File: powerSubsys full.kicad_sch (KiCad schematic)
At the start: 67 parts, among them J1 Conn_02x16_Odd_Even, J2 JST_PH_2mm, Q1 PN2222A, Q3 IRLML6402, U1 INA219AxD, U10 TPS63020DSJR, U2 DRV8833PWR, U3 BQ24074RGT, U4 TPS22810DRV, U5 TPS22810DRV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

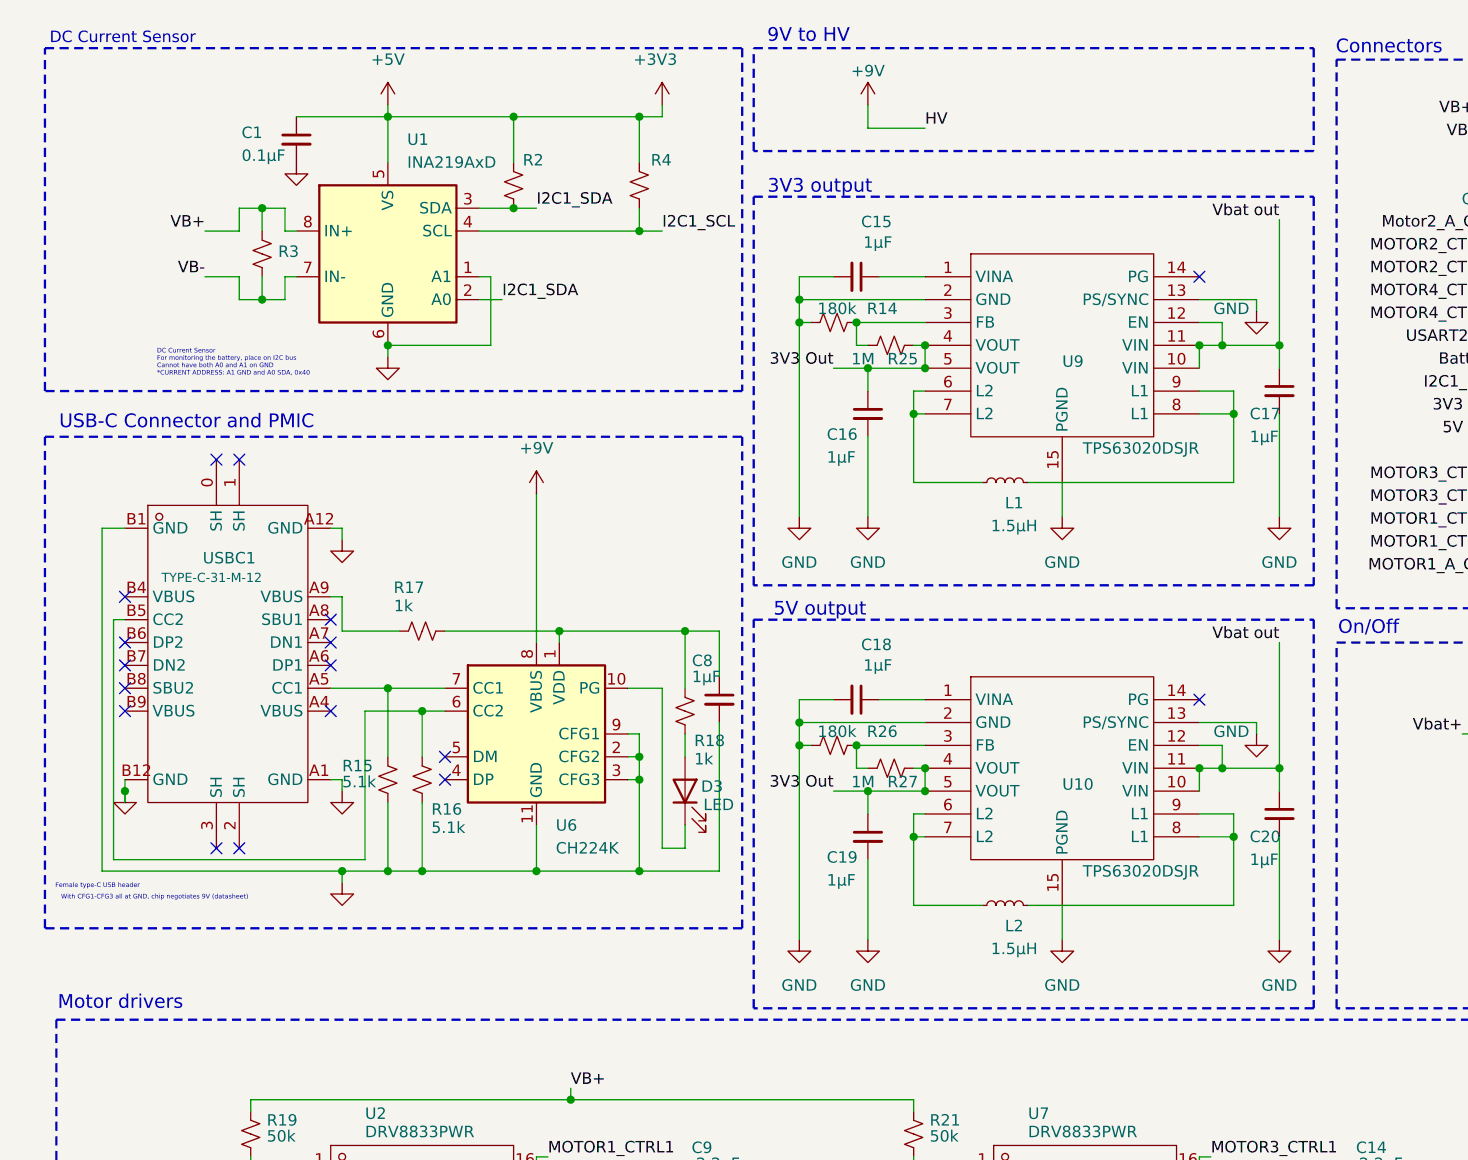
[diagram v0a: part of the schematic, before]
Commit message: Added 3V3 and 5V Output
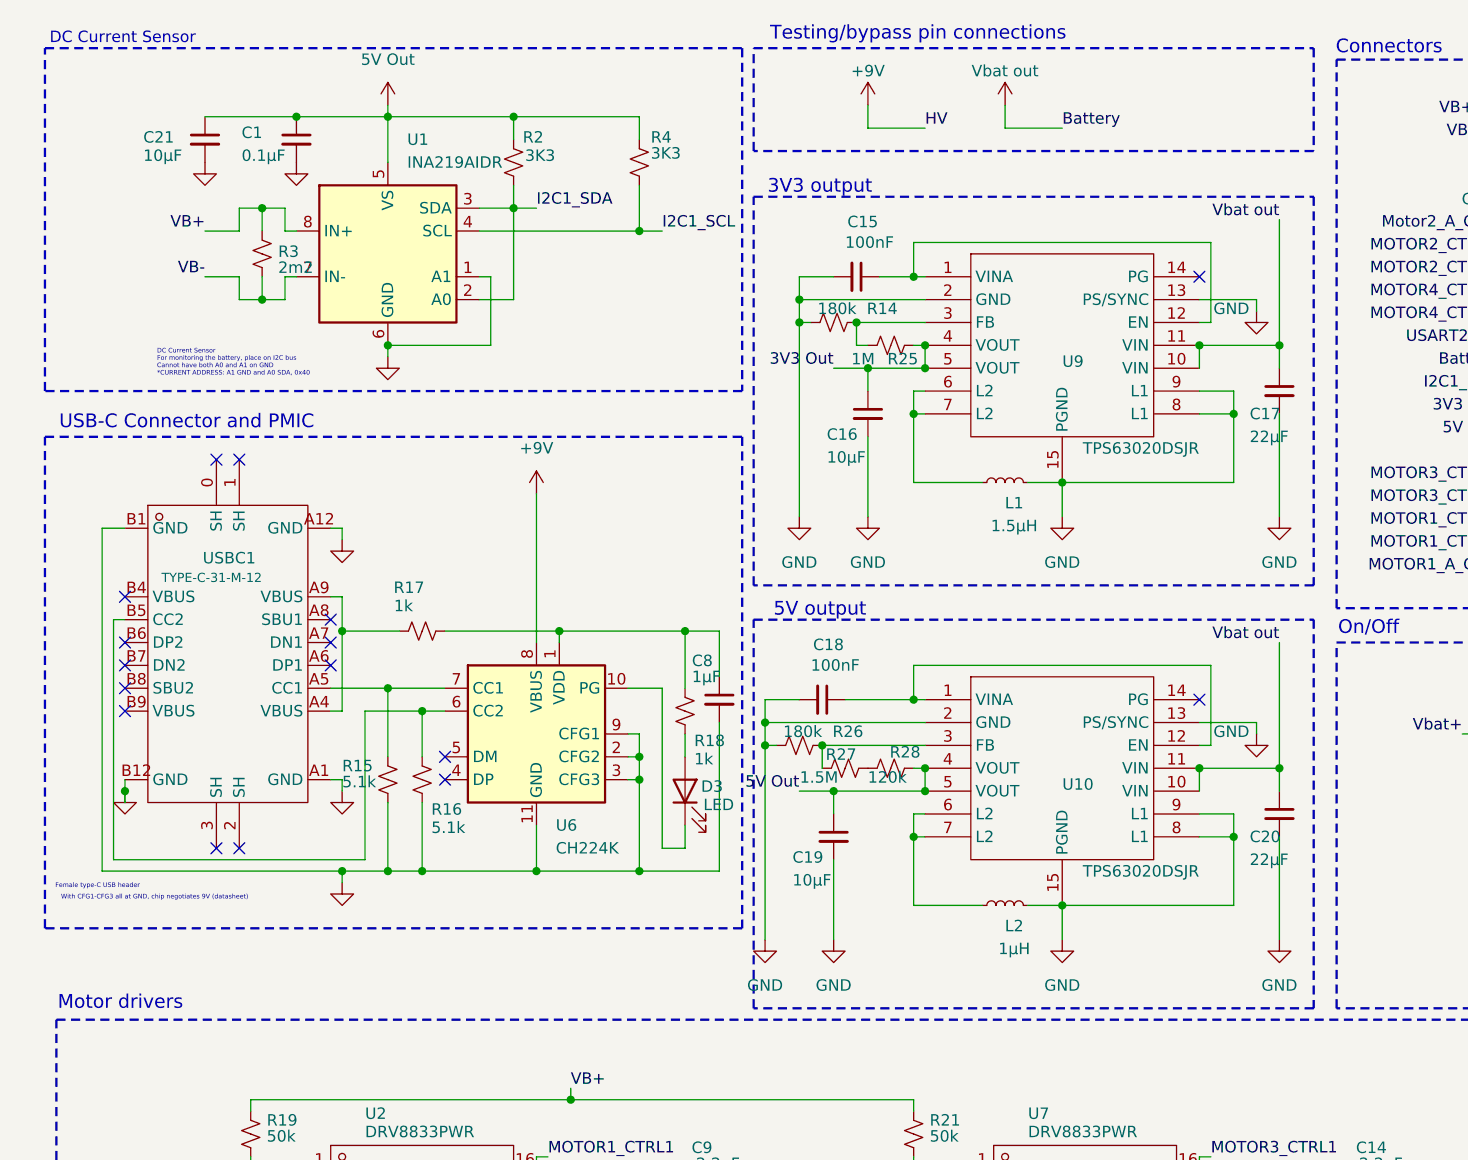
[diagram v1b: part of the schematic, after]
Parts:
- added C21: 10μF, symbol Device:C_Small
- added R28: 120k, symbol Device:R_Small_US
- C15, C18: value 1μF -> 100nF
- C16, C19: value 1μF -> 10μF
- C17, C20: value 1μF -> 22μF
- L2: value 1.5μH -> 1μH
- R2, R4: value R_Small_US -> 3K3
- R27: value 1M -> 1.5M
- R3: value R_Small_US -> 2m2
- U1: value INA219AxD -> INA219AIDR
- U10, U9: footprint VSON-14_L4.0-W3.0-P0.50-BL-EP_TI_DSJ -> Library:VSON-14_L4.0-W3.0-P0.50-BL-EP_TI_DSJ
- U2, U7: footprint TSSOP-16_L5.0-W4.4-P0.65-LS6.4-BL -> Library:TSSOP-16_L5.0-W4.4-P0.65-LS6.4-BL
- USBC1: footprint USB-C_SMD-TYPE-C-31-M-12 -> Library:USB-C_SMD-TYPE-C-31-M-12
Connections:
- net +3V3 is gone; now on net 5V Out: C1.1, R2.1, R4.1, U1.5 (VS)
- net Battery is gone; now on net Vbat out: J1.14 (Pin_14)
- net 3V3 Out: no longer C19.1, R27.2, U10.4 (VOUT), U10.5 (VOUT)
- net 5V Out: now also C19.1, U10.4 (VOUT), U10.5 (VOUT), C21.1, R28.2
- net GND: now also L1.2, L2.2, U10.8 (L1), U10.9 (L1), U9.8 (L1), U9.9 (L1), C21.2
- net Vbat out: no longer U10.12 (EN), U9.12 (EN)
- net at C18.1, U10.1 (VINA): now also U10.12 (EN)
- net at R17.1, USBC1.A9 (VBUS): now also USBC1.A4 (VBUS)
- net at C15.1, U9.1 (VINA): now also U9.12 (EN)
- new net: R27.2, R28.1
- no-connect marks 21 -> 20
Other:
- note added: "Testing/bypass pin connections"
- note removed: "9V to HV"
- moved on the sheet: R2, R4

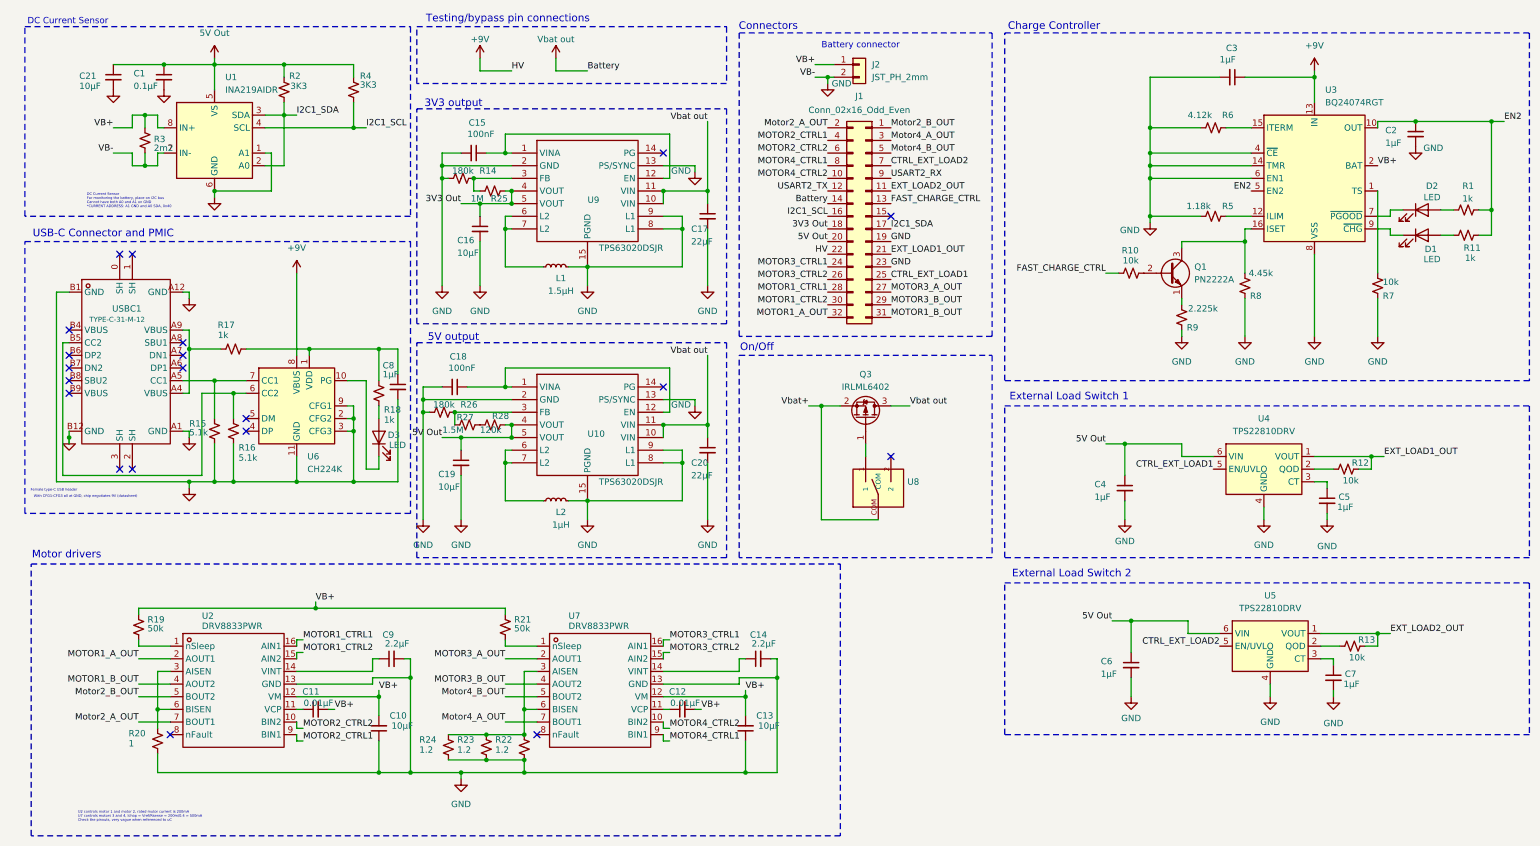
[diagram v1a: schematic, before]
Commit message: Updated the switch design
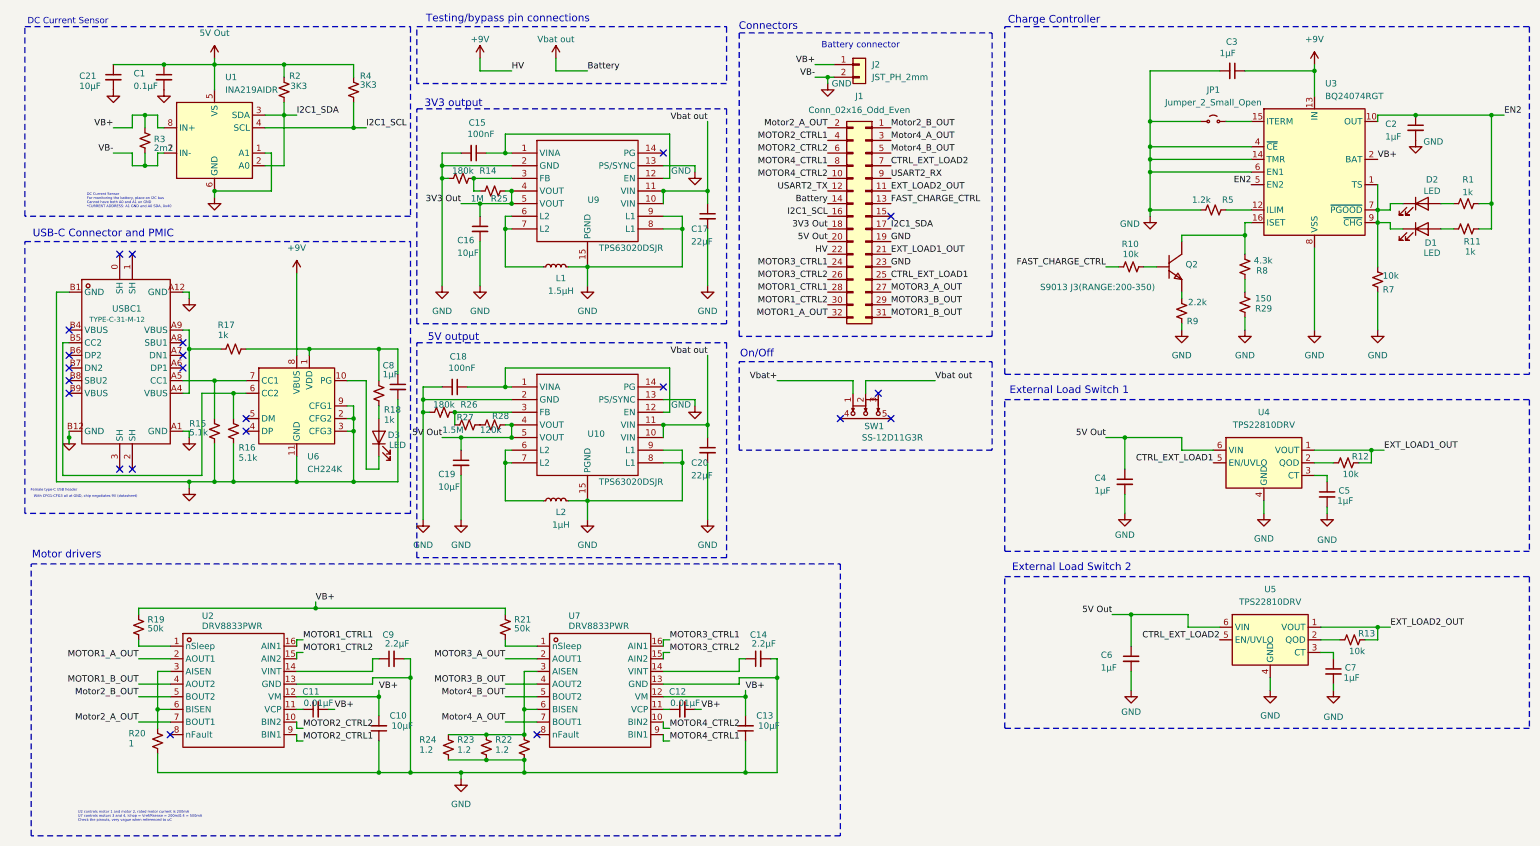
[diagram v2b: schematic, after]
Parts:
- removed Q1: PN2222A, Package_TO_SOT_THT:TO-92_Inline, symbol Transistor_BJT:PN2222A
- removed Q3: IRLML6402, Package_TO_SOT_SMD:SOT-23, symbol Transistor_FET:IRLML6402
- removed R6: 4.12k, symbol Device:R_Small_US
- removed U8: ~, SK12D07VG4:SK12D07VG4, symbol SK12D07VG4:SK12D07VG4
- added JP1: Jumper_2_Small_Open, symbol Jumper:Jumper_2_Small_Open
- added Q2: S9013 J3(RANGE:200-350), SOT-23-3_L2.9-W1.3-P1.90-LS2.4-BR, symbol S9013 J31_S9013 J3-altium-import:root_0_S9013 J3(RANGE{colon}200-350)_
- added R29: 150, symbol Device:R_Small_US
- added SW1: SS-12D11G3R, SW-TH_SS-12D11L3, symbol SS-12D11G3R1_SS-12D11G3R-altium-import:root_0_SS-12D11G3R_
- R5: value 1.18k -> 1.2k
- R8: value 4.45k -> 4.3k
- R9: value 2.225k -> 2.2k
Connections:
- net GND: now also JP1.1 (A), R29.2; no longer R8.2
- net Vbat out: now also SW1.2
- net Vbat+: now also SW1.1
- net at R9.1: now also Q2.2 (E)
- net at R10.2: now also Q2.1 (B)
- net at R8.1, U3.16 (ISET): now also Q2.3 (C)
- net at D2.1 (K), U3.7 (~{PGOOD}): now also D1.1 (K), R7.1, U3.1 (TS), U3.9 (~{CHG})
- net at U3.15 (ITERM): now also JP1.2 (B)
- new net: R29.1, R8.2
- no-connect marks 20 -> 22
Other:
- moved on the sheet: C2, C3, C4, C5, C6, C7, D1, D2, R1, R10, R11, R12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

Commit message: Updated the load switches
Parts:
- added C22, C23: 100nF, symbol Device:C_Small
- C5, C7: value 1μF -> 10nF
- U4, U5: value TPS22810DRV -> TPS22810DRVR
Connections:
- net Vbat+ is gone; now on net VB+: SW1.1
- net EXT_LOAD1_OUT: now also C22.1
- net EXT_LOAD2_OUT: now also C23.1
- net GND: now also C22.2, C23.2
- new net: D2.1 (K), U3.7 (~{PGOOD})
- new net: D1.1 (K), U3.9 (~{CHG})
- new net: R7.1, U3.1 (TS)
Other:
- moved on the sheet: C4, C5, C6, C7, R12, R13, U4, U5
